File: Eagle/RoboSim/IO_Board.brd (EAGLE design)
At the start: 100 x 80 mm, 66 parts, among them IC1 74HC595N, IC2 74LS165N, IC3 74HC595N, IC4 74HC595N, IC5 OPAMP-DUALDIP

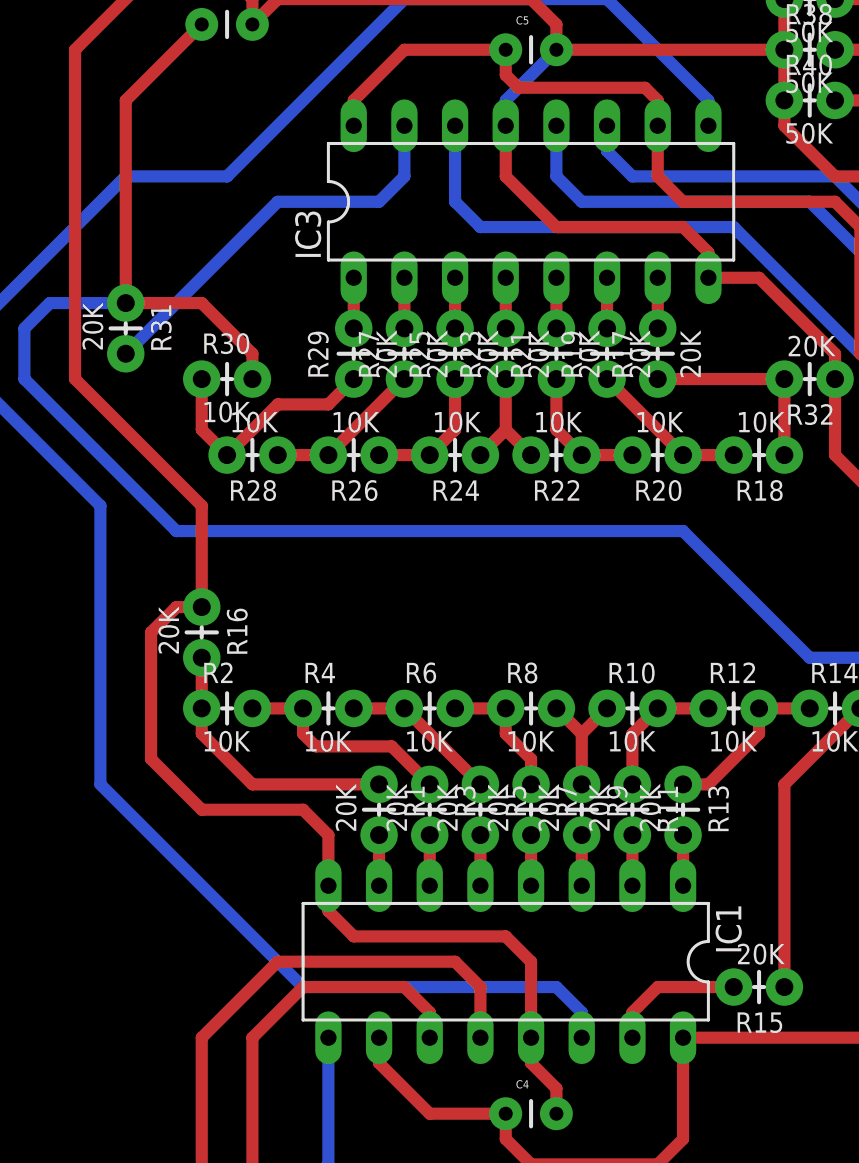
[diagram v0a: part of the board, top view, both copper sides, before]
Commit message: updated wiring diagram for DAC's. added fast io functions to arduino code. Added test vector generation. Still tuning good compromise between signal fedility and processor load
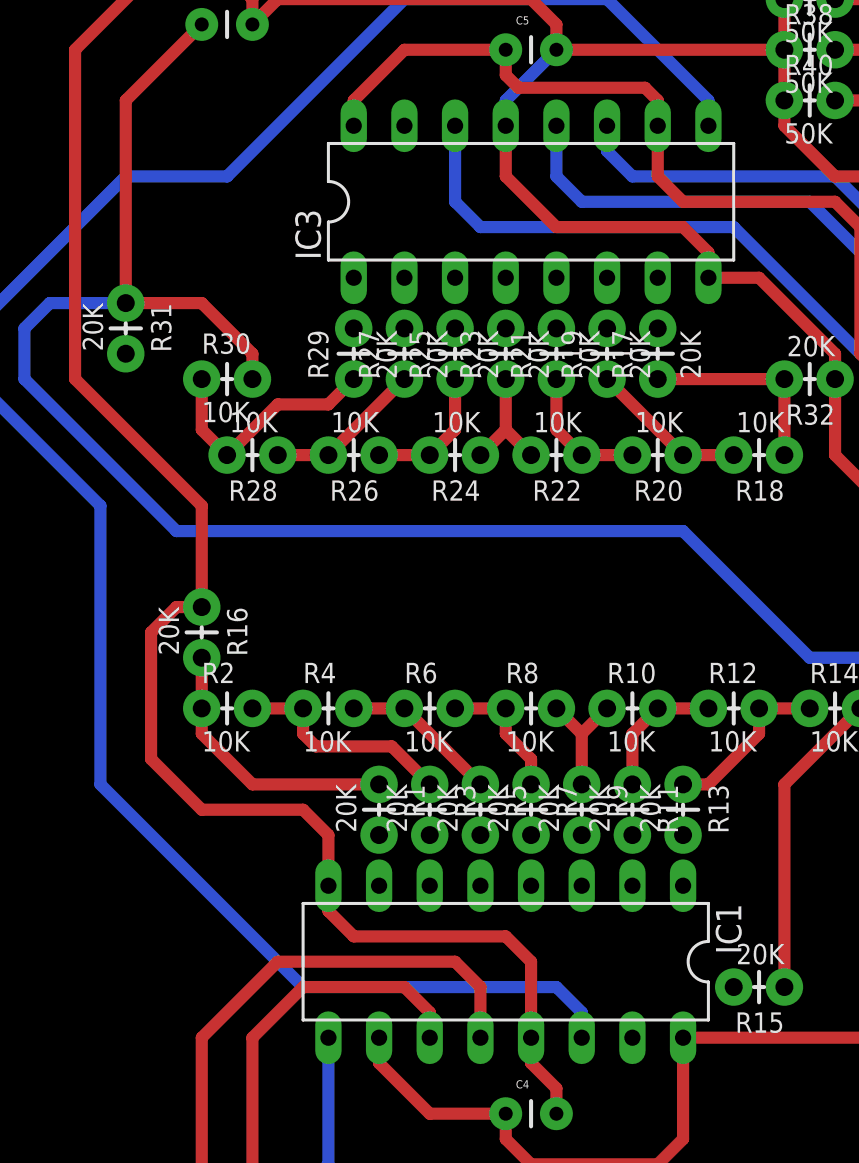
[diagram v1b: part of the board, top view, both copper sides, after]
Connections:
- net N$1: now also IC1.7; no longer IC1.15
- net N$19: now also IC3.7; no longer IC3.15
- net N$20: now also IC3.6; no longer IC3.1
- net N$21: now also IC3.5; no longer IC3.2
- net N$22: now also IC3.4; no longer IC3.3
- net N$23: now also IC3.3; no longer IC3.4
- net N$24: now also IC3.2; no longer IC3.5
- net N$25: now also IC3.1; no longer IC3.6
- net N$26: now also IC3.15; no longer IC3.7
- net N$3: now also IC1.6; no longer IC1.1
- net N$4: now also IC1.5; no longer IC1.2
- net N$5: now also IC1.4; no longer IC1.3
- net N$6: now also IC1.3; no longer IC1.4
- net N$7: now also IC1.2; no longer IC1.5
- net N$8: now also IC1.1; no longer IC1.6
- net N$9: now also IC1.15; no longer IC1.7
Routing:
- net N$19: track 20.2 -> 0.00 mm
- net N$1: track 6.88 -> 0.00 mm
- net N$9: track 2.54 -> 0.00 mm
- net N$8: track 2.54 -> 0.00 mm
- net N$7: track 2.54 -> 0.00 mm
- net N$6: track 2.54 -> 0.00 mm
- net N$5: track 2.54 -> 0.00 mm
- net N$4: track 2.54 -> 0.00 mm
- net N$3: track 2.54 -> 0.00 mm
- net N$26: track 2.54 -> 0.00 mm
- net N$25: track 2.54 -> 0.00 mm
- net N$24: track 2.54 -> 0.00 mm
- net N$23: track 2.54 -> 0.00 mm
- net N$22: track 2.54 -> 0.00 mm
- net N$21: track 2.54 -> 0.00 mm
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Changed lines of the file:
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@@
 <?xml version="1.0" encoding="utf-8"?>
 <!DOCTYPE eagle SYSTEM "eagle.dtd">
-<eagle version="6.5.0">
+<eagle version="7.3.0">
 <drawing>
 <settings>
@@
 <pass name="Default">
 <param name="RoutingGrid" value="50mil"/>
+<param name="AutoGrid" value="1"/>
+<param name="Efforts" value="0"/>
+<param name="TopRouterVariant" value="1"/>
 <param name="tpViaShape" value="round"/>
 <param name="PrefDir.1" value="|"/>
@@
 <wire x1="89.9922" y1="41.91" x2="90.17" y2="41.7322" width="0.6096" layer="1"/>
 </signal>
-<signal name="N$1">
-<contactref element="R15" pad="P$2"/>
-<contactref element="IC1" pad="15"/>
-<wire x1="35.56" y1="19.05" x2="35.56" y2="20.32" width="0.6096" layer="1"/>
-<wire x1="35.56" y1="20.32" x2="36.83" y2="21.59" width="0.6096" layer="1"/>
-<wire x1="36.83" y1="21.59" x2="40.64" y2="21.59" width="0.6096" layer="1"/>
-</signal>
-<signal name="N$3">
-<contactref element="R13" pad="P$2"/>
-<contactref element="IC1" pad="1"/>
-<wire x1="38.1" y1="29.21" x2="38.1" y2="26.67" width="0.6096" layer="1"/>
-</signal>
-<signal name="N$4">
-<contactref element="R11" pad="P$2"/>
-<contactref element="IC1" pad="2"/>
-<wire x1="35.56" y1="29.21" x2="35.56" y2="26.67" width="0.6096" layer="1"/>
-</signal>
-<signal name="N$5">
-<contactref element="R9" pad="P$2"/>
-<contactref element="IC1" pad="3"/>
-<wire x1="33.02" y1="29.21" x2="33.02" y2="26.67" width="0.6096" layer="1"/>
-</signal>
-<signal name="N$6">
-<contactref element="R7" pad="P$2"/>
-<contactref element="IC1" pad="4"/>
-<wire x1="30.48" y1="29.21" x2="30.48" y2="26.67" width="0.6096" layer="1"/>
-</signal>
-<signal name="N$7">
-<contactref element="R5" pad="P$2"/>
-<contactref element="IC1" pad="5"/>
-<wire x1="27.94" y1="29.21" x2="27.94" y2="26.67" width="0.6096" layer="1"/>
-</signal>
-<signal name="N$8">
-<contactref element="R3" pad="P$2"/>
-<contactref element="IC1" pad="6"/>
-<wire x1="25.4" y1="29.21" x2="25.4" y2="26.67" width="0.6096" layer="1"/>
-</signal>
-<signal name="N$9">
-<contactref element="R1" pad="P$2"/>
-<contactref element="IC1" pad="7"/>
-<wire x1="22.86" y1="29.21" x2="22.86" y2="26.67" width="0.6096" layer="1"/>
-</signal>
 <signal name="N$10">
 <contactref element="R1" pad="P$1"/>
@@
 <wire x1="90.17" y1="46.99" x2="94.1578" y2="46.99" width="0.6096" layer="1"/>
 <wire x1="94.1578" y1="46.99" x2="96.52" y2="44.6278" width="0.6096" layer="1"/>
-</signal>
-<signal name="N$19">
-<contactref element="R31" pad="P$2"/>
-<contactref element="IC3" pad="15"/>
-<wire x1="24.13" y1="64.77" x2="24.13" y2="62.23" width="0.6096" layer="16"/>
-<wire x1="24.13" y1="62.23" x2="22.86" y2="60.96" width="0.6096" layer="16"/>
-<wire x1="22.86" y1="60.96" x2="17.78" y2="60.96" width="0.6096" layer="16"/>
-<wire x1="17.78" y1="60.96" x2="10.16" y2="53.34" width="0.6096" layer="16"/>
-</signal>
-<signal name="N$20">
-<contactref element="R29" pad="P$2"/>
-<contactref element="IC3" pad="1"/>
-<wire x1="21.59" y1="54.61" x2="21.59" y2="57.15" width="0.6096" layer="1"/>
-</signal>
-<signal name="N$21">
-<contactref element="R27" pad="P$2"/>
-<contactref element="IC3" pad="2"/>
-<wire x1="24.13" y1="54.61" x2="24.13" y2="57.15" width="0.6096" layer="1"/>
-</signal>
-<signal name="N$22">
-<contactref element="R25" pad="P$2"/>
-<contactref element="IC3" pad="3"/>
-<wire x1="26.67" y1="54.61" x2="26.67" y2="57.15" width="0.6096" layer="1"/>
-</signal>
-<signal name="N$23">
-<contactref element="R23" pad="P$2"/>
-<contactref element="IC3" pad="4"/>
-<wire x1="29.21" y1="54.61" x2="29.21" y2="57.15" width="0.6096" layer="1"/>
-</signal>
-<signal name="N$24">
-<contactref element="R21" pad="P$2"/>
-<contactref element="IC3" pad="5"/>
-<wire x1="31.75" y1="54.61" x2="31.75" y2="57.15" width="0.6096" layer="1"/>
-</signal>
-<signal name="N$25">
-<contactref element="R19" pad="P$2"/>
-<contactref element="IC3" pad="6"/>
-<wire x1="34.29" y1="54.61" x2="34.29" y2="57.15" width="0.6096" layer="1"/>
-</signal>
-<signal name="N$26">
-<contactref element="R17" pad="P$2"/>
-<contactref element="IC3" pad="7"/>
-<wire x1="36.83" y1="54.61" x2="36.83" y2="57.15" width="0.6096" layer="1"/>
 </signal>
 <signal name="N$27">
@@
 <wire x1="95.25" y1="57.15" x2="90.17" y2="57.15" width="0.6096" layer="1"/>
 </signal>
+<signal name="N$1">
+<contactref element="IC1" pad="7"/>
+<contactref element="R15" pad="P$2"/>
+<wire x1="22.86" y1="26.67" x2="40.64" y2="21.59" width="0" layer="19" extent="1-1"/>
+</signal>
+<signal name="N$3">
+<contactref element="IC1" pad="6"/>
+<contactref element="R13" pad="P$2"/>
+<wire x1="25.4" y1="26.67" x2="38.1" y2="29.21" width="0" layer="19" extent="1-1"/>
+</signal>
+<signal name="N$4">
+<contactref element="IC1" pad="5"/>
+<contactref element="R11" pad="P$2"/>
+<wire x1="27.94" y1="26.67" x2="35.56" y2="29.21" width="0" layer="19" extent="1-1"/>
+</signal>
+<signal name="N$5">
+<contactref element="IC1" pad="4"/>
+<contactref element="R9" pad="P$2"/>
+<wire x1="30.48" y1="26.67" x2="33.02" y2="29.21" width="0" layer="19" extent="1-1"/>
+</signal>
+<signal name="N$6">
+<contactref element="IC1" pad="3"/>
+<contactref element="R7" pad="P$2"/>
+<wire x1="30.48" y1="29.21" x2="33.02" y2="26.67" width="0" layer="19" extent="1-1"/>
+</signal>
+<signal name="N$7">
+<contactref element="IC1" pad="2"/>
+<contactref element="R5" pad="P$2"/>
+<wire x1="27.94" y1="29.21" x2="35.56" y2="26.67" width="0" layer="19" extent="1-1"/>
+</signal>
+<signal name="N$8">
+<contactref element="IC1" pad="1"/>
+<contactref element="R3" pad="P$2"/>
+<wire x1="25.4" y1="29.21" x2="38.1" y2="26.67" width="0" layer="19" extent="1-1"/>
+</signal>
+<signal name="N$9">
+<contactref element="IC1" pad="15"/>
+<contactref element="R1" pad="P$2"/>
+<wire x1="22.86" y1="29.21" x2="35.56" y2="19.05" width="0" layer="19" extent="1-1"/>
+</signal>
+<signal name="N$19">
+<contactref element="IC3" pad="7"/>
+<contactref element="R31" pad="P$2"/>
+<wire x1="10.16" y1="53.34" x2="36.83" y2="57.15" width="0" layer="19" extent="1-1"/>
+</signal>
+<signal name="N$20">
+<contactref element="IC3" pad="6"/>
+<contactref element="R29" pad="P$2"/>
+<wire x1="21.59" y1="54.61" x2="34.29" y2="57.15" width="0" layer="19" extent="1-1"/>
+</signal>
+<signal name="N$21">
+<contactref element="IC3" pad="5"/>
+<contactref element="R27" pad="P$2"/>
+<wire x1="24.13" y1="54.61" x2="31.75" y2="57.15" width="0" layer="19" extent="1-1"/>
+</signal>
+<signal name="N$22">
+<contactref element="IC3" pad="4"/>
+<contactref element="R25" pad="P$2"/>
+<wire x1="26.67" y1="54.61" x2="29.21" y2="57.15" width="0" layer="19" extent="1-1"/>
+</signal>
+<signal name="N$23">
+<contactref element="IC3" pad="3"/>
+<contactref element="R23" pad="P$2"/>
+<wire x1="29.21" y1="54.61" x2="26.67" y2="57.15" width="0" layer="19" extent="1-1"/>
+</signal>
+<signal name="N$24">
+<contactref element="IC3" pad="2"/>
+<contactref element="R21" pad="P$2"/>
+<wire x1="24.13" y1="57.15" x2="31.75" y2="54.61" width="0" layer="19" extent="1-1"/>
+</signal>
+<signal name="N$25">
+<contactref element="IC3" pad="1"/>
+<contactref element="R19" pad="P$2"/>
+<wire x1="21.59" y1="57.15" x2="34.29" y2="54.61" width="0" layer="19" extent="1-1"/>
+</signal>
+<signal name="N$26">
+<contactref element="IC3" pad="15"/>
+<contactref element="R17" pad="P$2"/>
+<wire x1="24.13" y1="64.77" x2="36.83" y2="54.61" width="0" layer="19" extent="1-1"/>
+</signal>
 </signals>

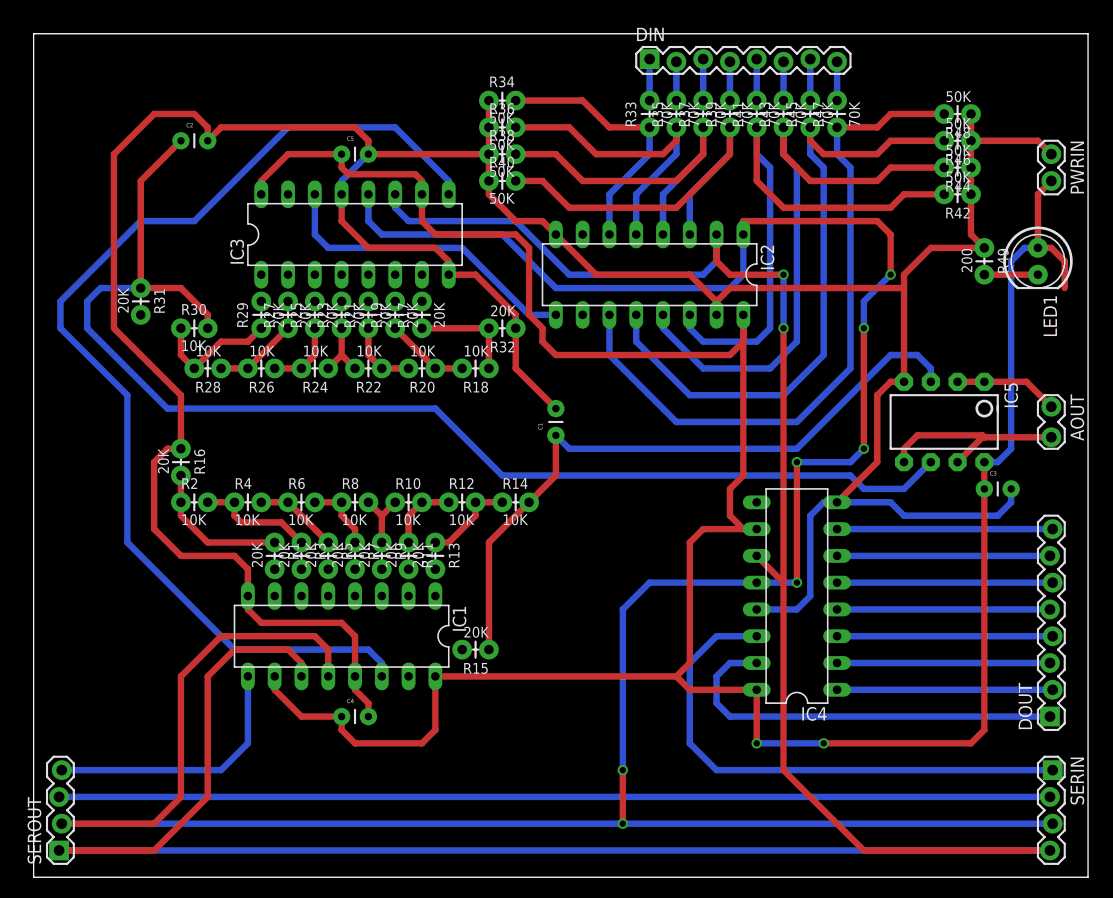
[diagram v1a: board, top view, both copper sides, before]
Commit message: Fixed issue with ch1 analog voltage follower. confirmed full board functionality
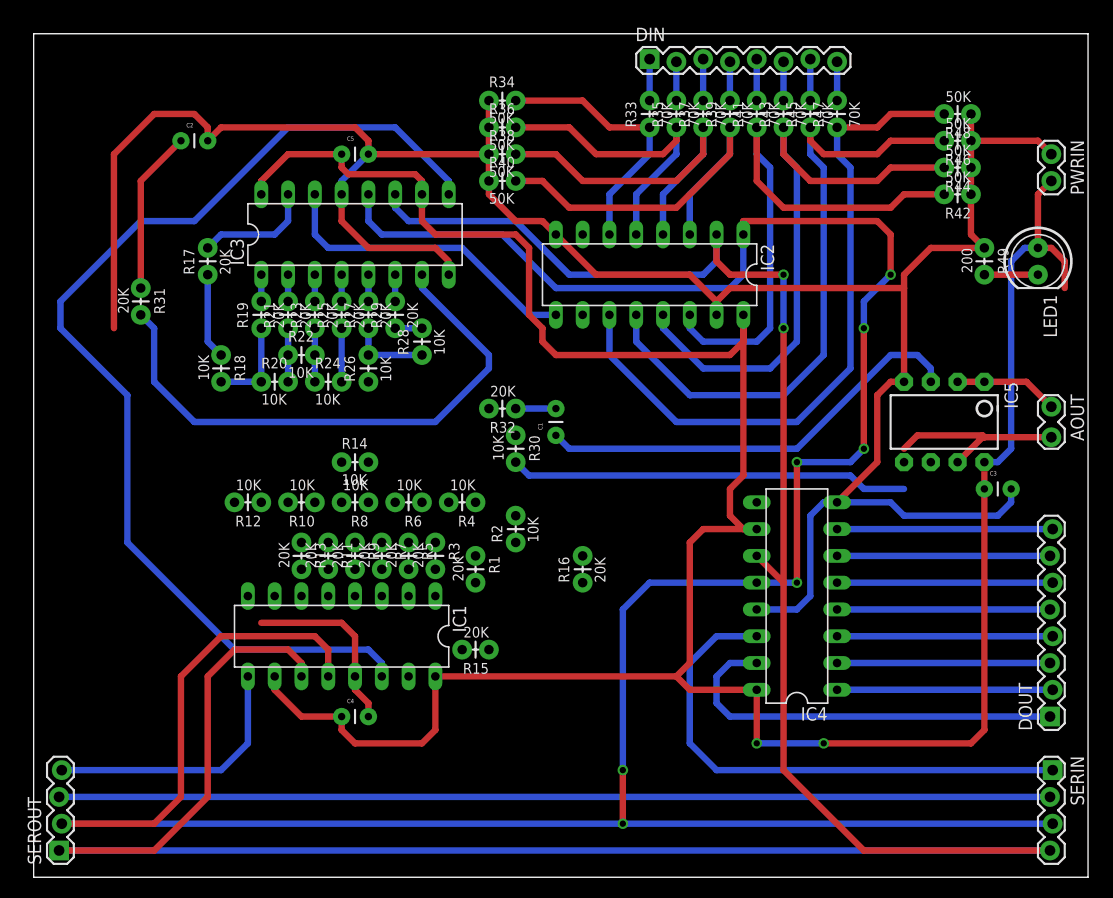
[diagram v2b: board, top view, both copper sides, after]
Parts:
- moved R16 40.2 mm to (52.1, 27.9), turned to 90 degrees
- moved R30 33.3 mm to (45.7, 41.9), turned to 270 degrees
- moved R2 32.0 mm to (45.7, 31.8), turned to 90 degrees
- moved R18 25.4 mm to (17.8, 49.5), turned to 270 degrees
- moved R4 22.9 mm to (41.9, 35.6), turned to 180 degrees
- moved R17 20.9 mm to (16.5, 57.1)
- moved R1 19.1 mm to (41.9, 30.5)
- moved R28 19.1 mm to (36.8, 49.5), turned to 90 degrees
- moved R12 17.8 mm to (21.6, 35.6), turned to 180 degrees
- moved R20 16.6 mm to (21.6, 47.0), turned to 0 degrees
- moved R14 15.7 mm to (29.2, 39.4)
- moved R13 12.7 mm to (25.4, 31.8)
- moved R3 12.7 mm to (38.1, 31.8)
- moved R19 12.7 mm to (21.6, 52.1)
- moved R29 12.7 mm to (34.3, 52.1)
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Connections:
- net N$2: now also IC5.6; no longer IC5.5
- net N$34: now also IC5.5; no longer IC5.6
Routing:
- net N$34: track 119.7 -> 53.4 mm
- net GND: track 298.1 -> 242.7 mm
- net N$19: track 0.00 -> 53.8 mm
- net N$17: track 64.5 -> 41.6 mm
- net N$10: track 13.8 -> 0.00 mm
- net N$11: track 11.2 -> 0.00 mm
- net N$26: track 0.00 -> 11.2 mm
- net N$33: track 12.3 -> 2.54 mm
- net N$16: track 8.67 -> 0.00 mm
- net N$12: track 7.93 -> 0.00 mm
- net N$13: track 6.88 -> 0.00 mm
- net N$15: track 6.88 -> 0.00 mm
- net N$14: track 6.13 -> 0.00 mm
- net N$25: track 0.00 -> 2.54 mm
- net N$24: track 0.00 -> 2.54 mm
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
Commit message: updated io board schematic, both PCB's ready for production
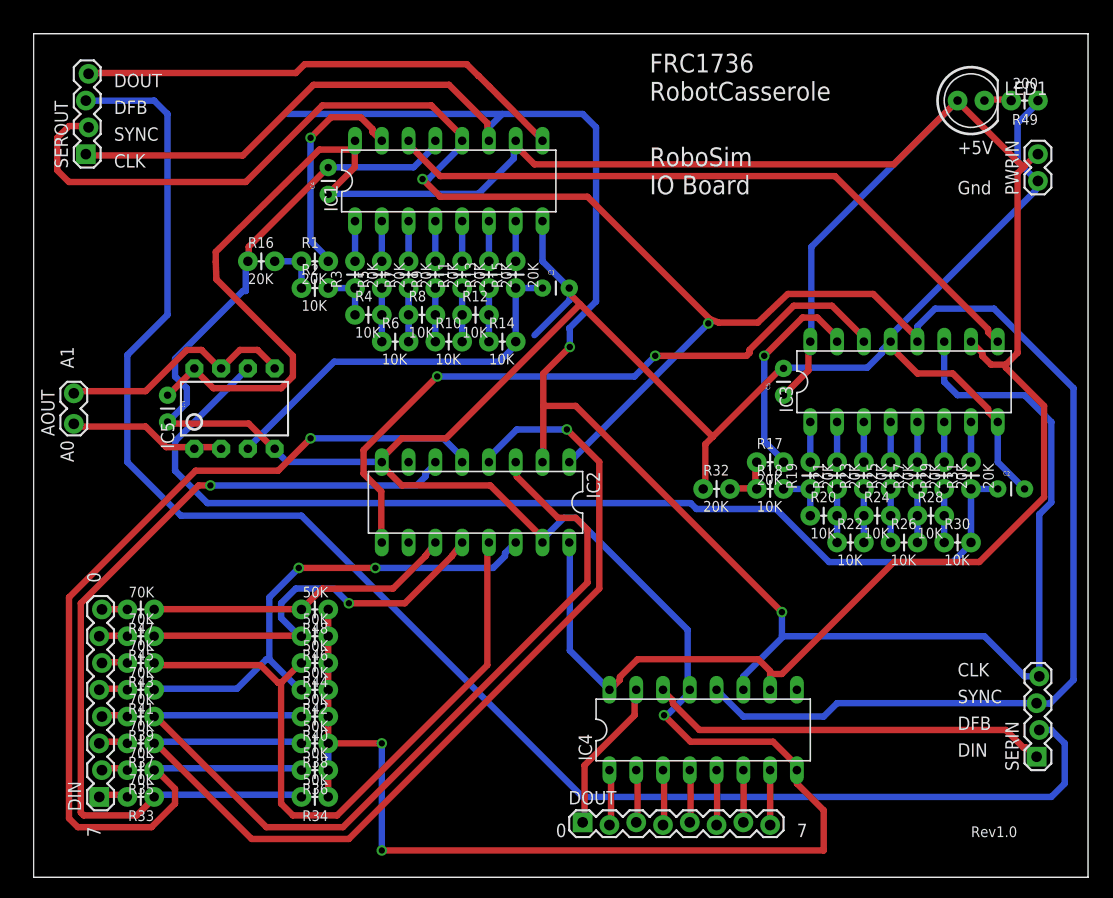
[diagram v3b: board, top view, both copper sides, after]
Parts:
- moved AOUT 92.7 mm to (3.81, 43.2), turned to 90 degrees
- moved DIN 87.1 mm to (6.35, 7.62), turned to 90 degrees
- moved C2 84.2 mm to (91.4, 36.8)
- moved R31 81.0 mm to (88.9, 36.8), turned to 90 degrees
- moved R47 79.3 mm to (11.4, 25.4), turned to 180 degrees
- moved R33 79.0 mm to (11.4, 7.62), turned to 180 degrees
- moved R45 78.8 mm to (11.4, 22.9), turned to 180 degrees
- moved R35 78.5 mm to (11.4, 10.2), turned to 180 degrees
- moved R43 78.4 mm to (11.4, 20.3), turned to 180 degrees
- moved R37 78.3 mm to (11.4, 12.7), turned to 180 degrees
- moved R41 78.2 mm to (11.4, 17.8), turned to 180 degrees
- moved R39 78.1 mm to (11.4, 15.2), turned to 180 degrees
- moved C3 78.0 mm to (12.7, 45.7), turned to 270 degrees
- moved R44 77.0 mm to (27.9, 20.3)
- moved R48 77.0 mm to (27.9, 25.4)
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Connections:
- net N$2: now also IC5.5; no longer IC5.6
- net N$34: now also IC5.6; no longer IC5.5
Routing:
- net GND: track 242.7 -> 348.7 mm, vias 0 -> 3
- net N$36: track 29.8 -> 95.6 mm, vias 0 -> 1
- net N$37: track 34.2 -> 95.5 mm, vias 0 -> 1
- net SYNC: track 274.8 -> 214.6 mm, vias 7 -> 2
- net DFB: track 94.0 -> 152.2 mm
- net N$35: track 25.5 -> 81.3 mm, vias 0 -> 1
- net N$19: track 53.8 -> 3.81 mm
- net N$38: track 37.8 -> 84.5 mm
- net N$34: track 53.4 -> 100.1 mm
- net CLK: track 259.2 -> 216.7 mm
- net N$63: track 102.7 -> 64.3 mm
- net N$42: track 65.5 -> 29.4 mm
- net N$60: track 29.8 -> 64.5 mm, vias 0 -> 2
- net N$43: track 39.0 -> 14.7 mm
- net N$41: track 61.1 -> 38.9 mm, vias 0 -> 1
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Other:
- board text added: "+5V"
- board text added: "0"
- board text added: "7"
- board text added: "A0"
- board text added: "A1"
- board text added: "CLK"
- board text added: "DFB"
- board text added: "DIN"
- board text added: "DOUT"
- board text added: "FRC1736 RobotCasserole"
- board text added: "Gnd"
- board text added: "Rev1.0"
- board text added: "RoboSim IO Board"
- board text added: "SYNC"
